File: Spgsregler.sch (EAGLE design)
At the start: 12 parts, among them X4_SPGSREGLER 22-23-2031, X5 22-23-2031

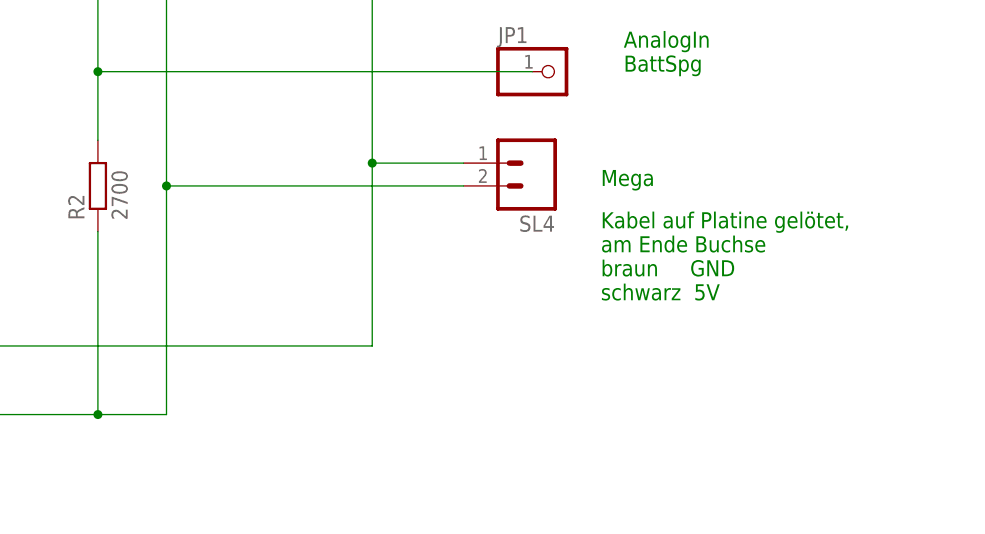
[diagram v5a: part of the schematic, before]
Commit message: 
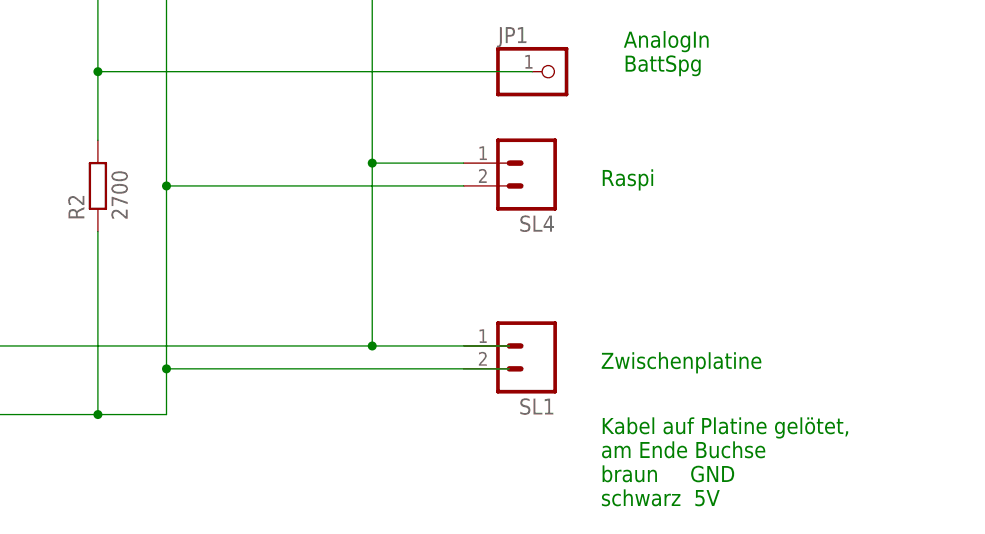
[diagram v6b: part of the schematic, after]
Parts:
- added SL1: (no value), con-amp-quick:M02
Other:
- note added: "Raspi"
- note added: "Zwischenplatine"
- note removed: "Mega"
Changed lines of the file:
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@@
 <part name="F1" library="fuse" deviceset="FUSE" device="BLANK_5X20MM"/>
 <part name="F3" library="fuse" deviceset="FUSE" device="BLANK_5X20MM"/>
+<part name="SL1" library="con-amp-quick" deviceset="M02" device=""/>
 </parts>
 <sheets>
@@
 <text x="134.62" y="96.52" size="1.778" layer="91" rot="R90">GND</text>
 <text x="137.16" y="96.52" size="1.778" layer="91" rot="MR90">5V</text>
-<text x="182.88" y="30.48" size="1.778" layer="91">Mega</text>
+<text x="182.88" y="30.48" size="1.778" layer="91">Raspi</text>
 <text x="182.88" y="60.96" size="1.778" layer="91">Nano</text>
 <text x="182.88" y="68.58" size="1.778" layer="91">Kabel auf Platine gelötet,
@@
 braun     GND
 schwarz  5V</text>
-<text x="182.88" y="17.78" size="1.778" layer="91">Kabel auf Platine gelötet,
+<text x="182.88" y="-5.08" size="1.778" layer="91">Kabel auf Platine gelötet,
 am Ende Buchse
 braun     GND
@@
 <text x="149.86" y="73.66" size="1.778" layer="91" rot="MR0">1.4A</text>
 <text x="10.16" y="50.8" size="1.778" layer="91" rot="MR270">4A</text>
+<text x="182.88" y="10.16" size="1.778" layer="91">Zwischenplatine</text>
 </plain>
 <instances>
@@
 <instance part="F1" gate="G$1" x="5.08" y="48.26" rot="R90"/>
 <instance part="F3" gate="G$1" x="147.32" y="78.74" rot="R180"/>
+<instance part="SL1" gate="G$1" x="175.26" y="12.7" rot="R180"/>
 </instances>
 <busses>
@@
 <pinref part="F3" gate="G$1" pin="1"/>
 <wire x1="157.48" y1="78.74" x2="152.4" y2="78.74" width="0.1524" layer="91"/>
+<wire x1="157.48" y1="12.7" x2="172.72" y2="12.7" width="0.1524" layer="91"/>
+<junction x="157.48" y="12.7"/>
 </segment>
 </net>
@@
 <wire x1="134.62" y1="83.82" x2="134.62" y2="60.96" width="0.1524" layer="91"/>
 <wire x1="134.62" y1="60.96" x2="134.62" y2="30.48" width="0.1524" layer="91"/>
-<wire x1="134.62" y1="30.48" x2="134.62" y2="5.08" width="0.1524" layer="91"/>
+<wire x1="134.62" y1="30.48" x2="134.62" y2="10.16" width="0.1524" layer="91"/>
 <pinref part="X4_SPGSREGLER" gate="-2" pin="S"/>
 <pinref part="SL2" gate="G$1" pin="2"/>
+<wire x1="134.62" y1="10.16" x2="134.62" y2="5.08" width="0.1524" layer="91"/>
 <wire x1="167.64" y1="60.96" x2="134.62" y2="60.96" width="0.1524" layer="91"/>
 <junction x="134.62" y="60.96"/>
@@
 <wire x1="127" y1="25.4" x2="127" y2="5.08" width="0.1524" layer="91"/>
 <junction x="127" y="5.08"/>
+<wire x1="172.72" y1="10.16" x2="134.62" y2="10.16" width="0.1524" layer="91"/>
+<junction x="134.62" y="10.16"/>
 </segment>
 </net>

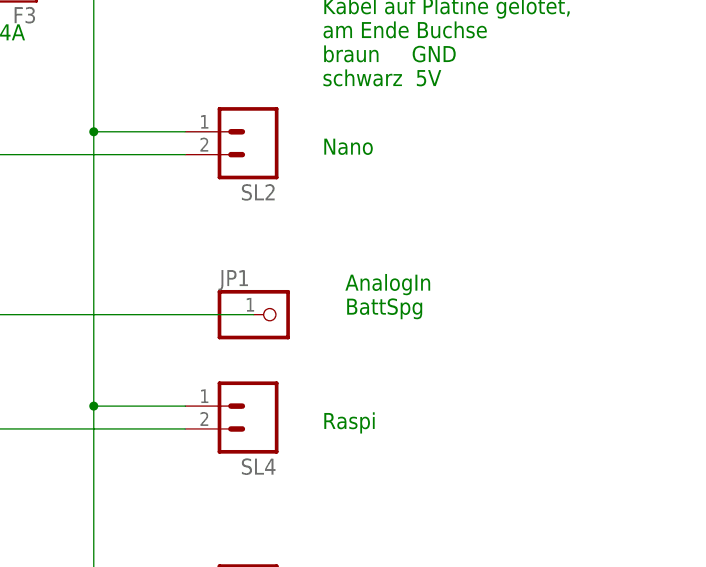
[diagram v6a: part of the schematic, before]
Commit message: 
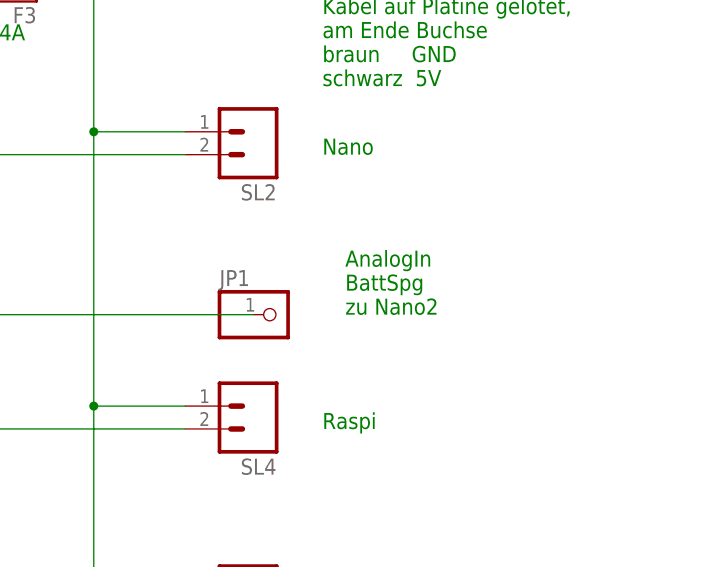
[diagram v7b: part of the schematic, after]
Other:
- note added: "AnalogIn BattSpg zu Nano2"
- note removed: "AnalogIn BattSpg"
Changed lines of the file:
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@@
 <text x="76.2" y="30.48" size="1.778" layer="91">MotorBoard</text>
 <text x="185.42" y="43.18" size="1.778" layer="91">AnalogIn
-BattSpg</text>
+BattSpg
+zu Nano2</text>
 <text x="114.3" y="96.52" size="1.778" layer="91">SpgsRegler</text>
 <text x="81.28" y="25.4" size="1.778" layer="91">12V</text>

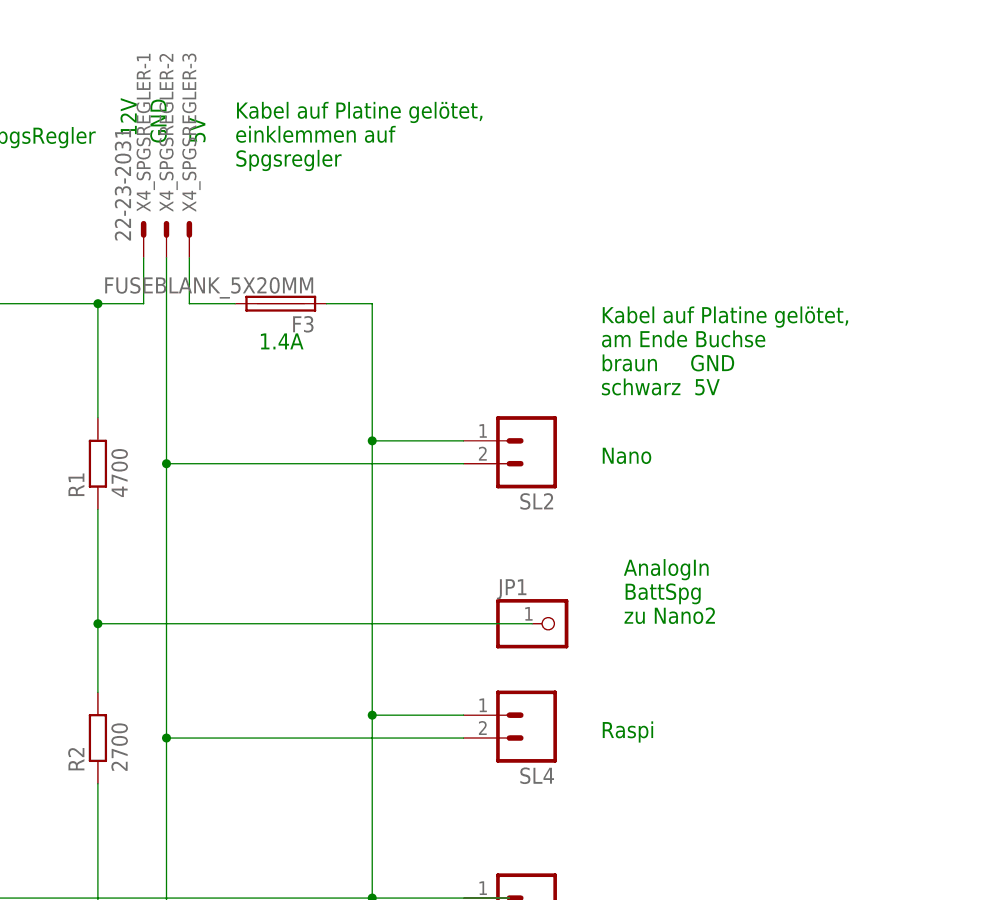
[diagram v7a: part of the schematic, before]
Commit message: 
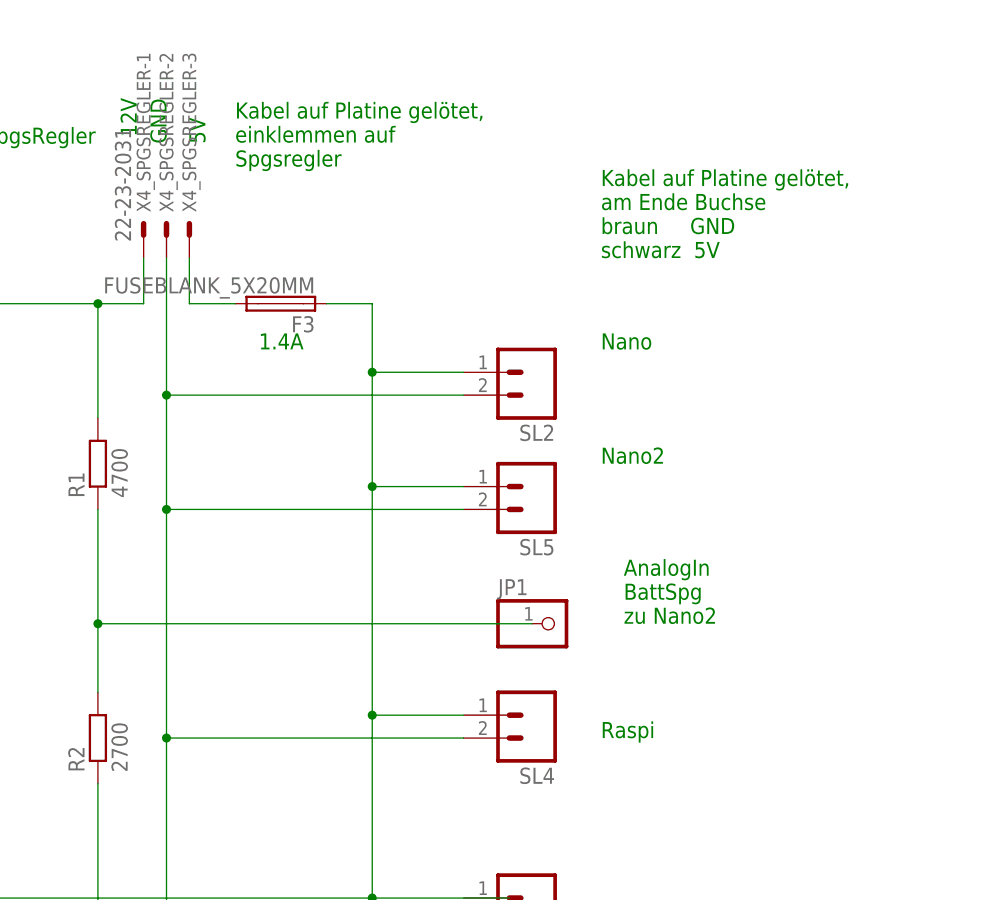
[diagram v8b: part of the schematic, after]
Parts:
- added SL5: (no value), con-amp-quick:M02
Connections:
- net N$2: now also SL5.2
- net N$6: now also SL5.1
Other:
- note added: "Nano2"
- moved on the sheet: SL2
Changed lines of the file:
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@@
 <part name="F3" library="fuse" deviceset="FUSE" device="BLANK_5X20MM"/>
 <part name="SL1" library="con-amp-quick" deviceset="M02" device=""/>
+<part name="SL5" library="con-amp-quick" deviceset="M02" device=""/>
 </parts>
 <sheets>
@@
 <text x="137.16" y="96.52" size="1.778" layer="91" rot="MR90">5V</text>
 <text x="182.88" y="30.48" size="1.778" layer="91">Raspi</text>
-<text x="182.88" y="60.96" size="1.778" layer="91">Nano</text>
-<text x="182.88" y="68.58" size="1.778" layer="91">Kabel auf Platine gelötet,
+<text x="182.88" y="73.66" size="1.778" layer="91">Nano</text>
+<text x="182.88" y="83.82" size="1.778" layer="91">Kabel auf Platine gelötet,
 am Ende Buchse
 braun     GND
@@
 <text x="10.16" y="50.8" size="1.778" layer="91" rot="MR270">4A</text>
 <text x="182.88" y="10.16" size="1.778" layer="91">Zwischenplatine</text>
+<text x="182.88" y="60.96" size="1.778" layer="91">Nano2</text>
 </plain>
 <instances>
@@
 <instance part="X5" gate="-3" x="73.66" y="20.32"/>
 <instance part="FRAME1" gate="G$1" x="-45.72" y="-45.72"/>
-<instance part="SL2" gate="G$1" x="175.26" y="63.5" rot="R180"/>
+<instance part="SL2" gate="G$1" x="175.26" y="71.12" rot="R180"/>
 <instance part="SL4" gate="G$1" x="175.26" y="33.02" rot="R180"/>
 <instance part="R1" gate="G$1" x="127" y="60.96" rot="R90"/>
@@
 <instance part="F3" gate="G$1" x="147.32" y="78.74" rot="R180"/>
 <instance part="SL1" gate="G$1" x="175.26" y="12.7" rot="R180"/>
+<instance part="SL5" gate="G$1" x="175.26" y="58.42" rot="R180"/>
 </instances>
 <busses>
@@
 <net name="N$6" class="0">
 <segment>
-<wire x1="157.48" y1="78.74" x2="157.48" y2="63.5" width="0.1524" layer="91"/>
-<wire x1="157.48" y1="63.5" x2="157.48" y2="33.02" width="0.1524" layer="91"/>
+<wire x1="157.48" y1="78.74" x2="157.48" y2="71.12" width="0.1524" layer="91"/>
+<wire x1="157.48" y1="71.12" x2="157.48" y2="58.42" width="0.1524" layer="91"/>
+<wire x1="157.48" y1="58.42" x2="157.48" y2="33.02" width="0.1524" layer="91"/>
 <wire x1="157.48" y1="33.02" x2="157.48" y2="12.7" width="0.1524" layer="91"/>
 <wire x1="157.48" y1="12.7" x2="68.58" y2="12.7" width="0.1524" layer="91"/>
 <wire x1="68.58" y1="12.7" x2="68.58" y2="20.32" width="0.1524" layer="91"/>
 <pinref part="SL2" gate="G$1" pin="1"/>
-<wire x1="167.64" y1="63.5" x2="157.48" y2="63.5" width="0.1524" layer="91"/>
-<junction x="157.48" y="63.5"/>
+<wire x1="167.64" y1="71.12" x2="157.48" y2="71.12" width="0.1524" layer="91"/>
+<junction x="157.48" y="71.12"/>
 <pinref part="SL4" gate="G$1" pin="1"/>
 <wire x1="167.64" y1="33.02" x2="157.48" y2="33.02" width="0.1524" layer="91"/>
@@
 <wire x1="157.48" y1="12.7" x2="172.72" y2="12.7" width="0.1524" layer="91"/>
 <junction x="157.48" y="12.7"/>
+<pinref part="SL5" gate="G$1" pin="1"/>
+<wire x1="167.64" y1="58.42" x2="157.48" y2="58.42" width="0.1524" layer="91"/>
+<junction x="157.48" y="58.42"/>
 </segment>
 </net>
@@
 <wire x1="134.62" y1="5.08" x2="127" y2="5.08" width="0.1524" layer="91"/>
 <wire x1="127" y1="5.08" x2="66.04" y2="5.08" width="0.1524" layer="91"/>
-<wire x1="134.62" y1="83.82" x2="134.62" y2="60.96" width="0.1524" layer="91"/>
-<wire x1="134.62" y1="60.96" x2="134.62" y2="30.48" width="0.1524" layer="91"/>
+<wire x1="134.62" y1="83.82" x2="134.62" y2="68.58" width="0.1524" layer="91"/>
+<wire x1="134.62" y1="68.58" x2="134.62" y2="55.88" width="0.1524" layer="91"/>
+<wire x1="134.62" y1="55.88" x2="134.62" y2="30.48" width="0.1524" layer="91"/>
 <wire x1="134.62" y1="30.48" x2="134.62" y2="10.16" width="0.1524" layer="91"/>
 <pinref part="X4_SPGSREGLER" gate="-2" pin="S"/>
 <pinref part="SL2" gate="G$1" pin="2"/>
 <wire x1="134.62" y1="10.16" x2="134.62" y2="5.08" width="0.1524" layer="91"/>
-<wire x1="167.64" y1="60.96" x2="134.62" y2="60.96" width="0.1524" layer="91"/>
-<junction x="134.62" y="60.96"/>
+<wire x1="167.64" y1="68.58" x2="134.62" y2="68.58" width="0.1524" layer="91"/>
+<junction x="134.62" y="68.58"/>
 <pinref part="SL4" gate="G$1" pin="2"/>
 <wire x1="167.64" y1="30.48" x2="134.62" y2="30.48" width="0.1524" layer="91"/>
@@
 <wire x1="172.72" y1="10.16" x2="134.62" y2="10.16" width="0.1524" layer="91"/>
 <junction x="134.62" y="10.16"/>
+<pinref part="SL5" gate="G$1" pin="2"/>
+<wire x1="167.64" y1="55.88" x2="134.62" y2="55.88" width="0.1524" layer="91"/>
+<junction x="134.62" y="55.88"/>
 </segment>
 </net>
